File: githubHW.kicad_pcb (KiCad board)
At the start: 2 copper layers, 99.7 x 99.1 mm, 146 parts, among them J1 Conn_01x06, J2 Conn_01x07, J3 Conn_01x07, J4 Conn_01x07, J5 Conn_01x07, J6 Conn_01x06, SW1 SW_Push, SW2 SW_Push, SW3 SW_Push, SW4 SW_Push, U1 WeMos_mini, U2 TPIC6B595N, U3 TLC5940NT, U4 TPIC6B595N

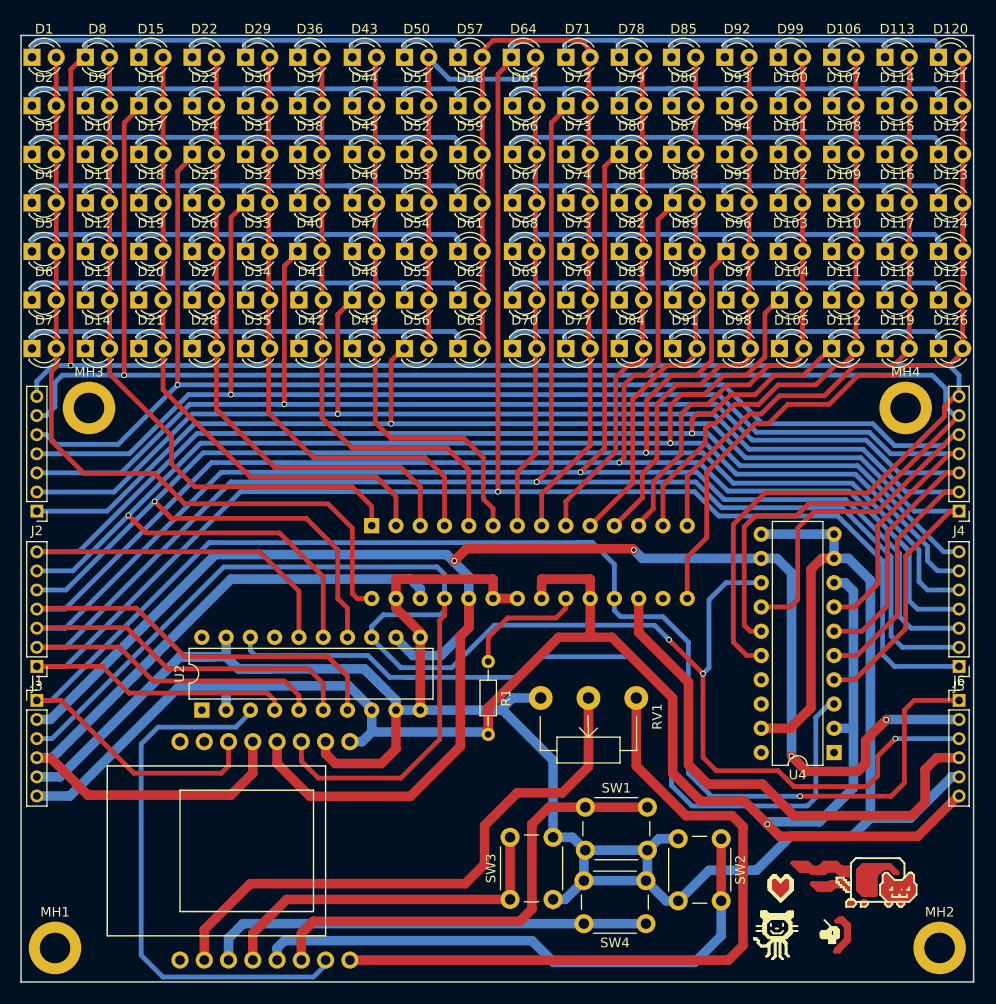
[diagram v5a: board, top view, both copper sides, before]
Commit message: scheme simplified for easier control
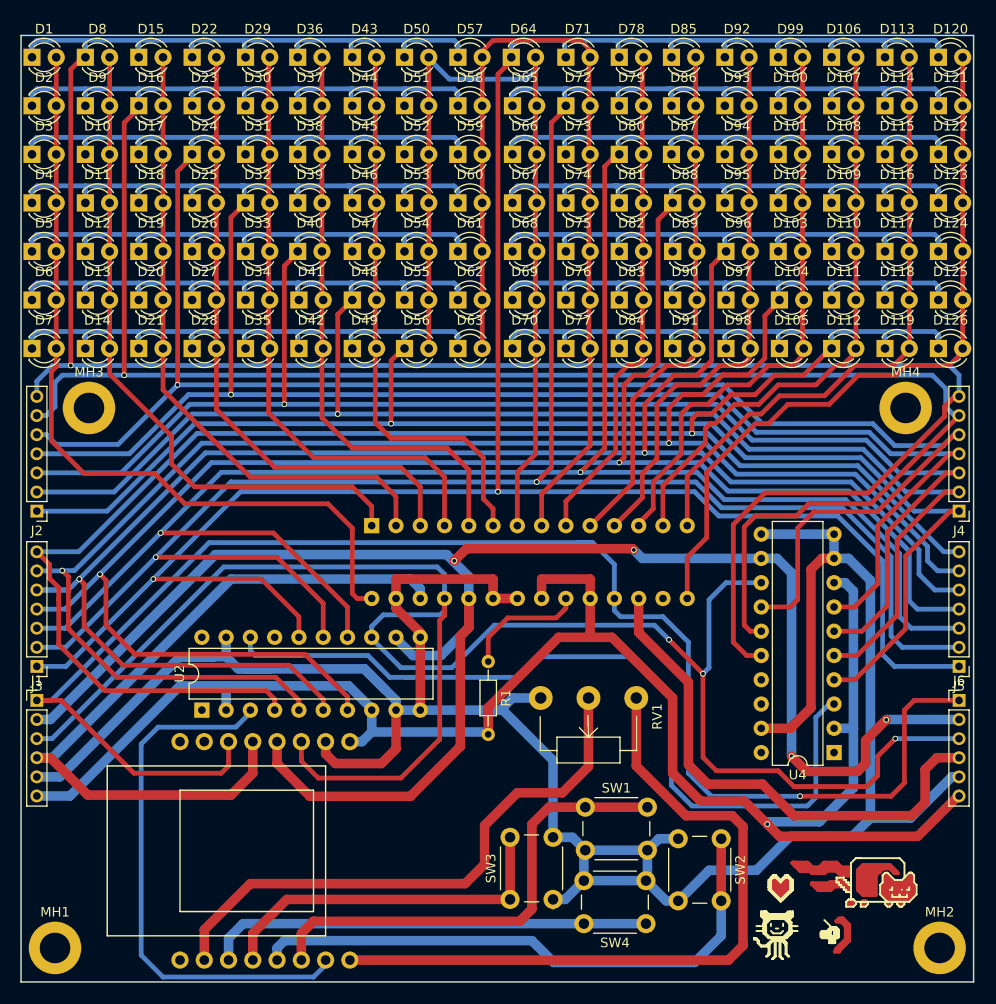
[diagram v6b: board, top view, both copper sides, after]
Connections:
- D1 pad 1: Net- -> Net-(D1-Pad1)
- D1 pad 2: Net- -> Net-(D1-Pad2)
- D10 pad 1: Net- -> Net-(D10-Pad1)
- D10 pad 2: Net- -> Net-(D10-Pad2)
- D100 pad 1: Net- -> Net-(D100-Pad1)
- D100 pad 2: Net- -> Net-(D100-Pad2)
- D101 pad 1: Net- -> Net-(D101-Pad1)
- D101 pad 2: Net- -> Net-(D100-Pad2)
- D102 pad 1: Net- -> Net-(D102-Pad1)
- D102 pad 2: Net- -> Net-(D100-Pad2)
- D103 pad 1: Net- -> Net-(D103-Pad1)
- D103 pad 2: Net- -> Net-(D100-Pad2)
- D104 pad 1: Net- -> Net-(D104-Pad1)
- D104 pad 2: Net- -> Net-(D100-Pad2)
- D105 pad 1: Net- -> Net-(D105-Pad1)
- D105 pad 2: Net- -> Net-(D100-Pad2)
- D106 pad 1: Net- -> Net-(D106-Pad1)
- D106 pad 2: Net- -> Net-(D106-Pad2)
- D107 pad 1: Net- -> Net-(D100-Pad1)
- D107 pad 2: Net- -> Net-(D106-Pad2)
- D108 pad 1: Net- -> Net-(D101-Pad1)
- D108 pad 2: Net- -> Net-(D106-Pad2)
- D109 pad 1: Net- -> Net-(D102-Pad1)
- D109 pad 2: Net- -> Net-(D106-Pad2)
- D11 pad 1: Net- -> Net-(D11-Pad1)
- D11 pad 2: Net- -> Net-(D10-Pad2)
- D110 pad 1: Net- -> Net-(D103-Pad1)
- D110 pad 2: Net- -> Net-(D106-Pad2)
- D111 pad 1: Net- -> Net-(D104-Pad1)
- D111 pad 2: Net- -> Net-(D106-Pad2)
- D112 pad 1: Net- -> Net-(D105-Pad1)
- D112 pad 2: Net- -> Net-(D106-Pad2)
- D113 pad 1: Net- -> Net-(D106-Pad1)
- D113 pad 2: Net- -> Net-(D113-Pad2)
- D114 pad 1: Net- -> Net-(D100-Pad1)
- D114 pad 2: Net- -> Net-(D113-Pad2)
- D115 pad 1: Net- -> Net-(D101-Pad1)
- D115 pad 2: Net- -> Net-(D113-Pad2)
- D116 pad 1: Net- -> Net-(D102-Pad1)
- D116 pad 2: Net- -> Net-(D113-Pad2)
- D117 pad 1: Net- -> Net-(D103-Pad1)
- D117 pad 2: Net- -> Net-(D113-Pad2)
- D118 pad 1: Net- -> Net-(D104-Pad1)
- D118 pad 2: Net- -> Net-(D113-Pad2)
- D119 pad 1: Net- -> Net-(D105-Pad1)
- D119 pad 2: Net- -> Net-(D113-Pad2)
- D12 pad 1: Net- -> Net-(D12-Pad1)
- D12 pad 2: Net- -> Net-(D10-Pad2)
- D120 pad 1: Net- -> Net-(D106-Pad1)
- D120 pad 2: Net- -> Net-(D120-Pad2)
- D121 pad 1: Net- -> Net-(D100-Pad1)
- D121 pad 2: Net- -> Net-(D120-Pad2)
- D122 pad 1: Net- -> Net-(D101-Pad1)
- D122 pad 2: Net- -> Net-(D120-Pad2)
- D123 pad 1: Net- -> Net-(D102-Pad1)
- D123 pad 2: Net- -> Net-(D120-Pad2)
- D124 pad 1: Net- -> Net-(D103-Pad1)
- D124 pad 2: Net- -> Net-(D120-Pad2)
- D125 pad 1: Net- -> Net-(D104-Pad1)
- D125 pad 2: Net- -> Net-(D120-Pad2)
- D126 pad 1: Net- -> Net-(D105-Pad1)
- D126 pad 2: Net- -> Net-(D120-Pad2)
- D13 pad 1: Net- -> Net-(D13-Pad1)
- D13 pad 2: Net- -> Net-(D10-Pad2)
- D14 pad 1: Net- -> Net-(D14-Pad1)
- D14 pad 2: Net- -> Net-(D10-Pad2)
- D15 pad 1: Net- -> Net-(D1-Pad1)
- D15 pad 2: Net- -> Net-(D15-Pad2)
- D16 pad 1: Net- -> Net-(D16-Pad1)
- D16 pad 2: Net- -> Net-(D15-Pad2)
- D17 pad 1: Net- -> Net-(D10-Pad1)
- D17 pad 2: Net- -> Net-(D15-Pad2)
- D18 pad 1: Net- -> Net-(D11-Pad1)
- D18 pad 2: Net- -> Net-(D15-Pad2)
- D19 pad 1: Net- -> Net-(D12-Pad1)
- D19 pad 2: Net- -> Net-(D15-Pad2)
- D2 pad 1: Net- -> Net-(D16-Pad1)
- D2 pad 2: Net- -> Net-(D1-Pad2)
- D20 pad 1: Net- -> Net-(D13-Pad1)
- D20 pad 2: Net- -> Net-(D15-Pad2)
- D21 pad 1: Net- -> Net-(D14-Pad1)
- D21 pad 2: Net- -> Net-(D15-Pad2)
- D22 pad 1: Net- -> Net-(D1-Pad1)
- D22 pad 2: Net- -> Net-(D22-Pad2)
- D23 pad 1: Net- -> Net-(D16-Pad1)
- D23 pad 2: Net- -> Net-(D22-Pad2)
- D24 pad 1: Net- -> Net-(D10-Pad1)
- D24 pad 2: Net- -> Net-(D22-Pad2)
- D25 pad 1: Net- -> Net-(D11-Pad1)
- D25 pad 2: Net- -> Net-(D22-Pad2)
- D26 pad 1: Net- -> Net-(D12-Pad1)
- D26 pad 2: Net- -> Net-(D22-Pad2)
- D27 pad 1: Net- -> Net-(D13-Pad1)
- D27 pad 2: Net- -> Net-(D22-Pad2)
- D28 pad 1: Net- -> Net-(D14-Pad1)
- D28 pad 2: Net- -> Net-(D22-Pad2)
- D29 pad 1: Net- -> Net-(D1-Pad1)
- D29 pad 2: Net- -> Net-(D29-Pad2)
- D3 pad 1: Net- -> Net-(D10-Pad1)
- D3 pad 2: Net- -> Net-(D1-Pad2)
- D30 pad 1: Net- -> Net-(D16-Pad1)
- D30 pad 2: Net- -> Net-(D29-Pad2)
- D31 pad 1: Net- -> Net-(D10-Pad1)
- D31 pad 2: Net- -> Net-(D29-Pad2)
- D32 pad 1: Net- -> Net-(D11-Pad1)
- D32 pad 2: Net- -> Net-(D29-Pad2)
- D33 pad 1: Net- -> Net-(D12-Pad1)
- D33 pad 2: Net- -> Net-(D29-Pad2)
- D34 pad 1: Net- -> Net-(D13-Pad1)
- D34 pad 2: Net- -> Net-(D29-Pad2)
- D35 pad 1: Net- -> Net-(D14-Pad1)
- D35 pad 2: Net- -> Net-(D29-Pad2)
- D36 pad 1: Net- -> Net-(D1-Pad1)
- D36 pad 2: Net- -> Net-(D36-Pad2)
- D37 pad 1: Net- -> Net-(D16-Pad1)
- D37 pad 2: Net- -> Net-(D36-Pad2)
- D38 pad 1: Net- -> Net-(D10-Pad1)
- D38 pad 2: Net- -> Net-(D36-Pad2)
- D39 pad 1: Net- -> Net-(D11-Pad1)
- D39 pad 2: Net- -> Net-(D36-Pad2)
- D4 pad 1: Net- -> Net-(D11-Pad1)
- D4 pad 2: Net- -> Net-(D1-Pad2)
- D40 pad 1: Net- -> Net-(D12-Pad1)
- D40 pad 2: Net- -> Net-(D36-Pad2)
- D41 pad 1: Net- -> Net-(D13-Pad1)
- D41 pad 2: Net- -> Net-(D36-Pad2)
- D42 pad 1: Net- -> Net-(D14-Pad1)
- D42 pad 2: Net- -> Net-(D36-Pad2)
- D43 pad 1: Net- -> Net-(D1-Pad1)
- D43 pad 2: Net- -> Net-(D43-Pad2)
- D44 pad 1: Net- -> Net-(D16-Pad1)
- D44 pad 2: Net- -> Net-(D43-Pad2)
- D45 pad 1: Net- -> Net-(D10-Pad1)
- D45 pad 2: Net- -> Net-(D43-Pad2)
- D46 pad 1: Net- -> Net-(D11-Pad1)
- D46 pad 2: Net- -> Net-(D43-Pad2)
- D47 pad 1: Net- -> Net-(D12-Pad1)
- D47 pad 2: Net- -> Net-(D43-Pad2)
- D48 pad 1: Net- -> Net-(D13-Pad1)
- D48 pad 2: Net- -> Net-(D43-Pad2)
- D49 pad 1: Net- -> Net-(D14-Pad1)
- D49 pad 2: Net- -> Net-(D43-Pad2)
- D5 pad 1: Net- -> Net-(D12-Pad1)
- D5 pad 2: Net- -> Net-(D1-Pad2)
- D50 pad 1: Net- -> Net-(D1-Pad1)
- D50 pad 2: Net- -> Net-(D50-Pad2)
- D51 pad 1: Net- -> Net-(D16-Pad1)
- D51 pad 2: Net- -> Net-(D50-Pad2)
- D52 pad 1: Net- -> Net-(D10-Pad1)
- D52 pad 2: Net- -> Net-(D50-Pad2)
- D53 pad 1: Net- -> Net-(D11-Pad1)
- D53 pad 2: Net- -> Net-(D50-Pad2)
- D54 pad 1: Net- -> Net-(D12-Pad1)
- D54 pad 2: Net- -> Net-(D50-Pad2)
- D55 pad 1: Net- -> Net-(D13-Pad1)
- D55 pad 2: Net- -> Net-(D50-Pad2)
- D56 pad 1: Net- -> Net-(D14-Pad1)
- D56 pad 2: Net- -> Net-(D50-Pad2)
- D57 pad 1: Net- -> Net-(D1-Pad1)
- D57 pad 2: Net- -> Net-(D57-Pad2)
- D58 pad 1: Net- -> Net-(D16-Pad1)
- D58 pad 2: Net- -> Net-(D57-Pad2)
- D59 pad 1: Net- -> Net-(D10-Pad1)
- D59 pad 2: Net- -> Net-(D57-Pad2)
- D6 pad 1: Net- -> Net-(D13-Pad1)
- D6 pad 2: Net- -> Net-(D1-Pad2)
- D60 pad 1: Net- -> Net-(D11-Pad1)
- D60 pad 2: Net- -> Net-(D57-Pad2)
- D61 pad 1: Net- -> Net-(D12-Pad1)
- D61 pad 2: Net- -> Net-(D57-Pad2)
- D62 pad 1: Net- -> Net-(D13-Pad1)
- D62 pad 2: Net- -> Net-(D57-Pad2)
- D63 pad 1: Net- -> Net-(D14-Pad1)
- D63 pad 2: Net- -> Net-(D57-Pad2)
- D64 pad 1: Net- -> Net-(D106-Pad1)
- D64 pad 2: Net- -> Net-(D50-Pad2)
- D65 pad 1: Net- -> Net-(D100-Pad1)
- D65 pad 2: Net- -> Net-(D50-Pad2)
- D66 pad 1: Net- -> Net-(D101-Pad1)
- D66 pad 2: Net- -> Net-(D50-Pad2)
- D67 pad 1: Net- -> Net-(D102-Pad1)
- D67 pad 2: Net- -> Net-(D50-Pad2)
- D68 pad 1: Net- -> Net-(D103-Pad1)
- D68 pad 2: Net- -> Net-(D50-Pad2)
- D69 pad 1: Net- -> Net-(D104-Pad1)
- D69 pad 2: Net- -> Net-(D50-Pad2)
- D7 pad 1: Net- -> Net-(D14-Pad1)
- D7 pad 2: Net- -> Net-(D1-Pad2)
- D70 pad 1: Net- -> Net-(D105-Pad1)
- D70 pad 2: Net- -> Net-(D50-Pad2)
- D71 pad 1: Net- -> Net-(D106-Pad1)
- D71 pad 2: Net- -> Net-(D57-Pad2)
- D72 pad 1: Net- -> Net-(D100-Pad1)
- D72 pad 2: Net- -> Net-(D57-Pad2)
- D73 pad 1: Net- -> Net-(D101-Pad1)
- D73 pad 2: Net- -> Net-(D57-Pad2)
- D74 pad 1: Net- -> Net-(D102-Pad1)
- D74 pad 2: Net- -> Net-(D57-Pad2)
- D75 pad 1: Net- -> Net-(D103-Pad1)
- D75 pad 2: Net- -> Net-(D57-Pad2)
- D76 pad 1: Net- -> Net-(D104-Pad1)
- D76 pad 2: Net- -> Net-(D57-Pad2)
- D77 pad 1: Net- -> Net-(D105-Pad1)
- D77 pad 2: Net- -> Net-(D57-Pad2)
- D78 pad 1: Net- -> Net-(D106-Pad1)
- D78 pad 2: Net- -> Net-(D78-Pad2)
- D79 pad 1: Net- -> Net-(D100-Pad1)
- D79 pad 2: Net- -> Net-(D78-Pad2)
- D8 pad 1: Net- -> Net-(D1-Pad1)
- D8 pad 2: Net- -> Net-(D10-Pad2)
- D80 pad 1: Net- -> Net-(D101-Pad1)
- D80 pad 2: Net- -> Net-(D78-Pad2)
- D81 pad 1: Net- -> Net-(D102-Pad1)
- D81 pad 2: Net- -> Net-(D78-Pad2)
- D82 pad 1: Net- -> Net-(D103-Pad1)
- D82 pad 2: Net- -> Net-(D78-Pad2)
- D83 pad 1: Net- -> Net-(D104-Pad1)
- D83 pad 2: Net- -> Net-(D78-Pad2)
- D84 pad 1: Net- -> Net-(D105-Pad1)
- D84 pad 2: Net- -> Net-(D78-Pad2)
- D85 pad 1: Net- -> Net-(D106-Pad1)
- D85 pad 2: Net- -> Net-(D85-Pad2)
- D86 pad 1: Net- -> Net-(D100-Pad1)
- D86 pad 2: Net- -> Net-(D85-Pad2)
- D87 pad 1: Net- -> Net-(D101-Pad1)
- D87 pad 2: Net- -> Net-(D85-Pad2)
- D88 pad 1: Net- -> Net-(D102-Pad1)
- D88 pad 2: Net- -> Net-(D85-Pad2)
- D89 pad 1: Net- -> Net-(D103-Pad1)
- D89 pad 2: Net- -> Net-(D85-Pad2)
- D9 pad 1: Net- -> Net-(D16-Pad1)
- D9 pad 2: Net- -> Net-(D10-Pad2)
- D90 pad 1: Net- -> Net-(D104-Pad1)
- D90 pad 2: Net- -> Net-(D85-Pad2)
- D91 pad 1: Net- -> Net-(D105-Pad1)
- D91 pad 2: Net- -> Net-(D85-Pad2)
- D92 pad 1: Net- -> Net-(D106-Pad1)
- D92 pad 2: Net- -> Net-(D92-Pad2)
- D93 pad 1: Net- -> Net-(D100-Pad1)
- D93 pad 2: Net- -> Net-(D92-Pad2)
- D94 pad 1: Net- -> Net-(D101-Pad1)
- D94 pad 2: Net- -> Net-(D92-Pad2)
- D95 pad 1: Net- -> Net-(D102-Pad1)
- D95 pad 2: Net- -> Net-(D92-Pad2)
- D96 pad 1: Net- -> Net-(D103-Pad1)
- D96 pad 2: Net- -> Net-(D92-Pad2)
- D97 pad 1: Net- -> Net-(D104-Pad1)
- D97 pad 2: Net- -> Net-(D92-Pad2)
- D98 pad 1: Net- -> Net-(D105-Pad1)
- D98 pad 2: Net- -> Net-(D92-Pad2)
- D99 pad 1: Net- -> Net-(D106-Pad1)
- D99 pad 2: Net- -> Net-(D100-Pad2)
- J1 pad 4: Net- -> Net-(J1-Pad4)
- J2 pad 1: Net- -> Net-(D14-Pad1)
- J2 pad 2: Net- -> Net-(D13-Pad1)
- J2 pad 3: Net- -> Net-(D12-Pad1)
- J2 pad 4: Net- -> Net-(D11-Pad1)
- J2 pad 5: Net- -> Net-(D10-Pad1)
- J2 pad 6: Net- -> Net-(D16-Pad1)
- J2 pad 7: Net- -> Net-(D1-Pad1)
- J3 pad 1: Net- -> Net-(D106-Pad1)
- J3 pad 2: Net- -> Net-(D100-Pad1)
- J3 pad 3: Net- -> Net-(D101-Pad1)
- J3 pad 4: Net- -> Net-(D102-Pad1)
- J3 pad 5: Net- -> Net-(D103-Pad1)
- J3 pad 6: Net- -> Net-(D104-Pad1)
- J3 pad 7: Net- -> Net-(D105-Pad1)
- J4 pad 1: Net- -> Net-(D14-Pad1)
- J4 pad 2: Net- -> Net-(D13-Pad1)
- J4 pad 3: Net- -> Net-(D12-Pad1)
- J4 pad 4: Net- -> Net-(D11-Pad1)
- J4 pad 5: Net- -> Net-(D10-Pad1)
- J4 pad 6: Net- -> Net-(D16-Pad1)
- J4 pad 7: Net- -> Net-(D1-Pad1)
- J5 pad 1: Net- -> Net-(D106-Pad1)
- J5 pad 2: Net- -> Net-(D100-Pad1)
- J5 pad 3: Net- -> Net-(D101-Pad1)
- J5 pad 4: Net- -> Net-(D102-Pad1)
- J5 pad 5: Net- -> Net-(D103-Pad1)
- J5 pad 6: Net- -> Net-(D104-Pad1)
- J5 pad 7: Net- -> Net-(D105-Pad1)
- J6 pad 4: Net- -> Net-(J6-Pad4)
- MH1 pad 1: (no net) -> Net-(MH1-Pad1)
- MH2 pad 1: (no net) -> Net-(MH2-Pad1)
- MH3 pad 1: (no net) -> Net-(MH3-Pad1)
- MH4 pad 1: (no net) -> Net-(MH4-Pad1)
- R1 pad 1: Net- -> Net-(R1-Pad1)
- RV1 pad 2: Net- -> Net-(RV1-Pad2)
- SW1 pad 1: Net- -> Net-(SW1-Pad1)
- SW2 pad 1: Net- -> Net-(SW2-Pad1)
- SW3 pad 1: Net- -> Net-(SW3-Pad1)
- SW4 pad 1: Net- -> Net-(SW4-Pad1)
- U1 pad 10: Net- -> Net-(RV1-Pad2)
- U1 pad 11: Net- -> Net-(SW4-Pad1)
- U1 pad 12: Net- -> Net-(SW3-Pad1)
- U1 pad 13: Net- -> Net-(SW2-Pad1)
- U1 pad 14: Net- -> Net-(SW1-Pad1)
- U1 pad 15: Net- -> Net-(U1-Pad15)
- U1 pad 5: Net- -> Net-(J1-Pad4)
- U1 pad 7: (no net) -> Net-(U1-Pad7)
- U1 pad 8: (no net) -> Net-(U1-Pad8)
- U1 pad 9: (no net) -> Net-(U1-Pad9)
- U2 pad 1: (no net) -> Net-(U2-Pad1)
- U2 pad 14: Net- -> Net-(D101-Pad1)
- U2 pad 15: Net- -> Net-(D100-Pad1)
- U2 pad 16: Net- -> Net-(D106-Pad1)
- U2 pad 17: (no net) -> Net-(U2-Pad17)
- U2 pad 18: Net- -> Net-(U2-Pad18)
- U2 pad 20: (no net) -> Net-(U2-Pad20)
- U2 pad 3: Net- -> Net-(U1-Pad15)
- U2 pad 4: Net- -> Net-(D105-Pad1)
- U2 pad 5: Net- -> Net-(D104-Pad1)
- U2 pad 6: Net- -> Net-(D103-Pad1)
- U2 pad 7: Net- -> Net-(D102-Pad1)
- U3 pad 1: Net- -> Net-(D10-Pad2)
- U3 pad 10: Net- -> Net-(D85-Pad2)
- U3 pad 11: Net- -> Net-(D92-Pad2)
- U3 pad 12: Net- -> Net-(D100-Pad2)
- U3 pad 13: Net- -> Net-(D106-Pad2)
- U3 pad 14: Net- -> Net-(D113-Pad2)
- U3 pad 15: Net- -> Net-(D120-Pad2)
- U3 pad 16: (no net) -> Net-(U3-Pad16)
- U3 pad 17: Net- -> Net-(J6-Pad4)
- U3 pad 2: Net- -> Net-(D15-Pad2)
- U3 pad 20: Net- -> Net-(R1-Pad1)
- U3 pad 26: Net- -> Net-(J1-Pad4)
- U3 pad 28: Net- -> Net-(D1-Pad2)
- U3 pad 3: Net- -> Net-(D22-Pad2)
- U3 pad 4: Net- -> Net-(D29-Pad2)
- U3 pad 5: Net- -> Net-(D36-Pad2)
- U3 pad 6: Net- -> Net-(D43-Pad2)
- U3 pad 7: Net- -> Net-(D50-Pad2)
- U3 pad 8: Net- -> Net-(D57-Pad2)
- U3 pad 9: Net- -> Net-(D78-Pad2)
- U4 pad 1: (no net) -> Net-(U4-Pad1)
- U4 pad 14: Net- -> Net-(D10-Pad1)
- U4 pad 15: Net- -> Net-(D16-Pad1)
- U4 pad 16: Net- -> Net-(D1-Pad1)
- U4 pad 17: (no net) -> Net-(U4-Pad17)
- U4 pad 18: (no net) -> Net-(U4-Pad18)
- U4 pad 20: (no net) -> Net-(U4-Pad20)
- U4 pad 3: Net- -> Net-(U2-Pad18)
- U4 pad 4: Net- -> Net-(D14-Pad1)
- U4 pad 5: Net- -> Net-(D13-Pad1)
- U4 pad 6: Net- -> Net-(D12-Pad1)
- U4 pad 7: Net- -> Net-(D11-Pad1)
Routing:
- net Net-: track 4818.2 -> 0.00 mm, vias 16 -> 0
- net Net-(D106-Pad1): track 0.00 -> 244.4 mm, vias 0 -> 2
- net Net-(D1-Pad1): track 0.00 -> 242.9 mm, vias 0 -> 1
- net Net-(D102-Pad1): track 0.00 -> 242.3 mm, vias 0 -> 2
- net Net-(D100-Pad1): track 0.00 -> 242.2 mm, vias 0 -> 2
- net Net-(D101-Pad1): track 0.00 -> 237.5 mm, vias 0 -> 2
- net Net-(D103-Pad1): track 0.00 -> 235.4 mm, vias 0 -> 2
- net Net-(D16-Pad1): track 0.00 -> 233.1 mm, vias 0 -> 1
- net Net-(D104-Pad1): track 0.00 -> 227.8 mm, vias 0 -> 2
- net Net-(D105-Pad1): track 0.00 -> 225.4 mm, vias 0 -> 1
- net Net-(D10-Pad1): track 0.00 -> 221.2 mm, vias 0 -> 1
- net Net-(D11-Pad1): track 0.00 -> 207.4 mm, vias 0 -> 1
- net Net-(D12-Pad1): track 0.00 -> 204.6 mm, vias 0 -> 1
- net Net-(D13-Pad1): track 0.00 -> 201.6 mm, vias 0 -> 1
- net Net-(D14-Pad1): track 0.00 -> 198.3 mm, vias 0 -> 1
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
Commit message: tux added ♥
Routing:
- net (no net): track 133.0 -> 161.6 mm
- net Net-(J6-Pad4): track 54.6 -> 52.9 mm
